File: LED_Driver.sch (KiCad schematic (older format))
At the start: 0 parts

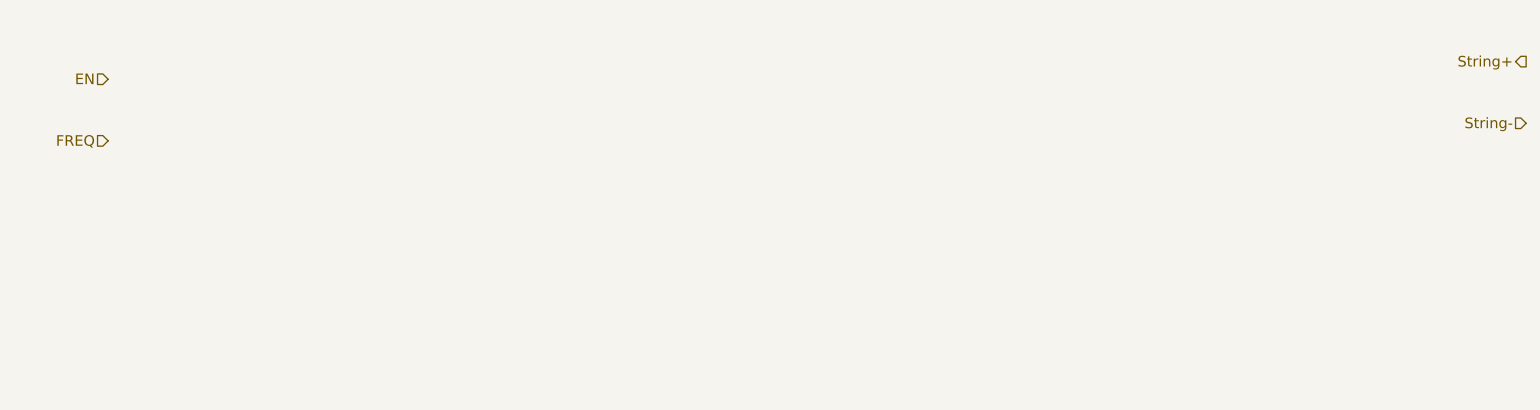
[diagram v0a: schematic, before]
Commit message: Changes up to and including Arduino module
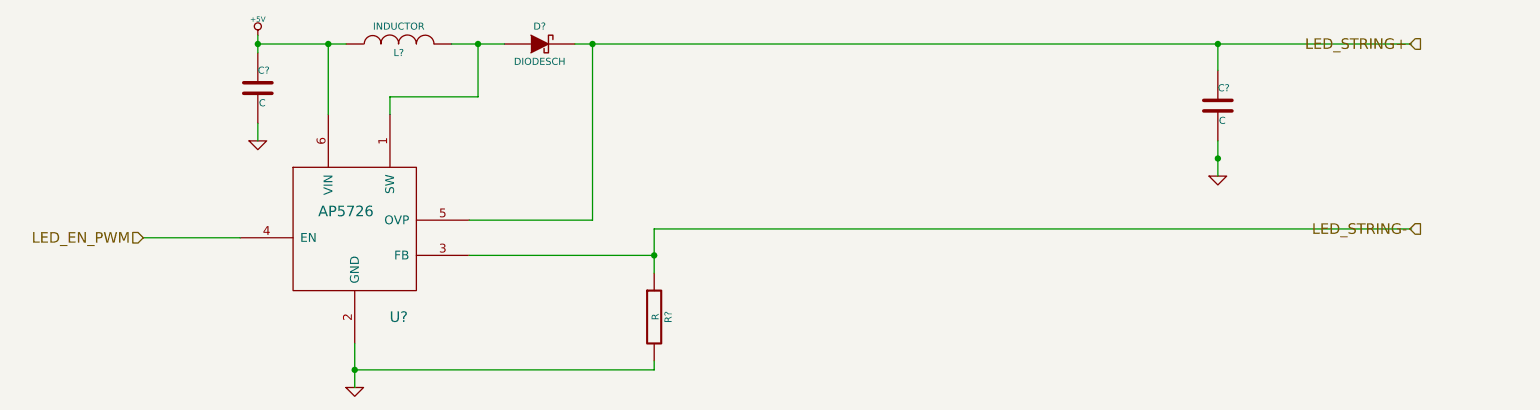
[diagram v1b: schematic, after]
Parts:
- added C? (x2): C, ~, symbol C
- added D?: DIODESCH, ~, symbol DIODESCH
- added L?: INDUCTOR, ~, symbol INDUCTOR
- added R?: R, ~, symbol R
- added U?: AP5726, symbol AP5726
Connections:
- net labels added: +5V, GND, LED_EN_PWM, LED_STRING+, LED_STRING-
- net labels removed: EN, FREQ, String+, String-
- wire segments 0 -> 20
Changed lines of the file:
@@
 LIBS:valves
 LIBS:BencyBuddy
+LIBS:arduino_shieldsNCL
 LIBS:BenchBuddy-cache
 EELAYER 27 0
@@
 Sheet 5 9
 Title ""
-Date "9 feb 2014"
+Date "12 feb 2014"
 Rev ""
 Comp ""
@@
 Comment4 ""
 $EndDescr
-Text HLabel 1950 1750 0    60   Input ~ 0
-EN
-Text HLabel 1950 2100 0    60   Input ~ 0
-FREQ
-Text HLabel 10000 1650 0    60   Output ~ 0
-String+
-Text HLabel 10000 2000 0    60   Input ~ 0
-String-
+Text HLabel 2150 2650 0    60   Input ~ 0
+LED_EN_PWM
+Text HLabel 9400 1550 0    60   Output ~ 0
+LED_STRING+
+Text HLabel 9400 2600 0    60   Output ~ 0
+LED_STRING-
+$Comp
+L AP5726 U?
+U 1 1 52F99132
+P 3350 2650
+F 0 "U?" H 3600 2200 60  0000 C CNN
+F 1 "AP5726" H 3300 2800 60  0000 C CNN
+F 2 "" H 3350 2600 60  0000 C CNN
+F 3 "" H 3350 2600 60  0000 C CNN
+	1    3350 2650
+	1    0    0    -1
+$EndComp
+$Comp
+L +5V #PWR?
+U 1 1 52F9981D
+P 2800 1500
+F 0 "#PWR?" H 2800 1590 20  0001 C CNN
+F 1 "+5V" H 2800 1590 30  0000 C CNN
+F 2 "" H 2800 1500 60  0000 C CNN
+F 3 "" H 2800 1500 60  0000 C CNN
+	1    2800 1500
+	1    0    0    -1
+$EndComp
+$Comp
+L GND #PWR?
+U 1 1 52F9982C
+P 2800 2100
+F 0 "#PWR?" H 2800 2100 30  0001 C CNN
+F 1 "GND" H 2800 2030 30  0001 C CNN
+F 2 "" H 2800 2100 60  0000 C CNN
+F 3 "" H 2800 2100 60  0000 C CNN
+	1    2800 2100
+	1    0    0    -1
+$EndComp
+$Comp
+L GND #PWR?
+U 1 1 52F99839
+P 3350 3500
+F 0 "#PWR?" H 3350 3500 30  0001 C CNN
+F 1 "GND" H 3350 3430 30  0001 C CNN
+F 2 "" H 3350 3500 60  0000 C CNN
+F 3 "" H 3350 3500 60  0000 C CNN
+	1    3350 3500
+	1    0    0    -1
+$EndComp
+$Comp
+L C C?
+U 1 1 52F99841
+P 2800 1800
+F 0 "C?" H 2800 1900 40  0000 L CNN
+F 1 "C" H 2806 1715 40  0000 L CNN
+F 2 "~" H 2838 1650 30  0000 C CNN
+F 3 "~" H 2800 1800 60  0000 C CNN
+	1    2800 1800
+	1    0    0    -1
+$EndComp
+Wire Wire Line
+	2800 1500 2800 1600
+Wire Wire Line
+	2800 2000 2800 2100
+Wire Wire Line
+	2800 1550 3300 1550
+Wire Wire Line
+	3200 1550 3200 1950
+Connection ~ 2800 1550
+$Comp
+L INDUCTOR L?
+U 1 1 52F99856
+P 3600 1550
+F 0 "L?" V 3550 1550 40  0000 C CNN
+F 1 "INDUCTOR" V 3700 1550 40  0000 C CNN
+F 2 "~" H 3600 1550 60  0000 C CNN
+F 3 "~" H 3600 1550 60  0000 C CNN
+	1    3600 1550
+	0    -1   -1   0
+$EndComp
+Connection ~ 3200 1550
+Wire Wire Line
+	3550 1950 3550 1850
+Wire Wire Line
+	3550 1850 4050 1850
+Wire Wire Line
+	4050 1850 4050 1550
+Wire Wire Line
+	3900 1550 4200 1550
+$Comp
+L DIODESCH D?
+U 1 1 52F99876
+P 4400 1550
+F 0 "D?" H 4400 1650 40  0000 C CNN
+F 1 "DIODESCH" H 4400 1450 40  0000 C CNN
+F 2 "~" H 4400 1550 60  0000 C CNN
+F 3 "~" H 4400 1550 60  0000 C CNN
+	1    4400 1550
+	1    0    0    -1
+$EndComp
+Connection ~ 4050 1550
+$Comp
+L C C?
+U 1 1 52F99898
+P 8250 1900
+F 0 "C?" H 8250 2000 40  0000 L CNN
+F 1 "C" H 8256 1815 40  0000 L CNN
+F 2 "~" H 8288 1750 30  0000 C CNN
+F 3 "~" H 8250 1900 60  0000 C CNN
+	1    8250 1900
+	1    0    0    -1
+$EndComp
+$Comp
+L GND #PWR?
+U 1 1 52F9989E
+P 8250 2300
+F 0 "#PWR?" H 8250 2300 30  0001 C CNN
+F 1 "GND" H 8250 2230 30  0001 C CNN
+F 2 "" H 8250 2300 60  0000 C CNN
+F 3 "" H 8250 2300 60  0000 C CNN
+	1    8250 2300
+	1    0    0    -1
+$EndComp
+Wire Wire Line
+	4600 1550 9350 1550
+Wire Wire Line
+	8250 1550 8250 1700
+Wire Wire Line
+	8250 2100 8250 2300
+Wire Wire Line
+	4700 2550 4700 1550
+Connection ~ 4700 1550
+Wire Wire Line
+	4000 2550 4700 2550
+Wire Wire Line
+	3350 3250 3350 3500
+Wire Wire Line
+	4000 2750 5050 2750
+$Comp
+L R R?
+U 1 1 52F99912
+P 5050 3100
+F 0 "R?" V 5130 3100 40  0000 C CNN
+F 1 "R" V 5057 3101 40  0000 C CNN
+F 2 "~" V 4980 3100 30  0000 C CNN
+F 3 "~" H 5050 3100 30  0000 C CNN
+	1    5050 3100
+	1    0    0    -1
+$EndComp
+Wire Wire Line
+	5050 3350 5050 3400
+Wire Wire Line
+	5050 3400 3350 3400
+Connection ~ 3350 3400
+Connection ~ 8250 2200
+Connection ~ 5050 2750
+Connection ~ 8250 1550
+Wire Wire Line
+	5050 2850 5050 2600
+Wire Wire Line
+	5050 2600 9350 2600
+Wire Wire Line
+	2150 2650 2700 2650
 $EndSCHEMATC
